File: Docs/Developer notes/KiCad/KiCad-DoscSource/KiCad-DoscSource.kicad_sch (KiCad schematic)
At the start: 0 parts

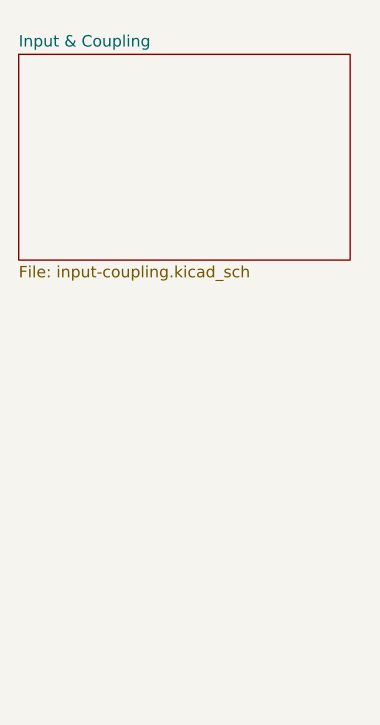
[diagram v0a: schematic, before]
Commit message: Add attenuator to developer notes
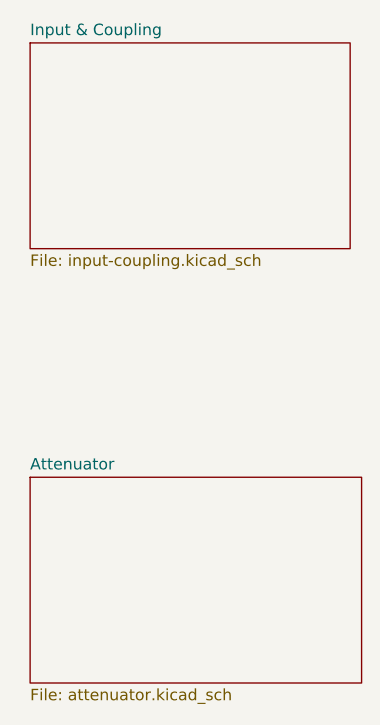
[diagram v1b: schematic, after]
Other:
- added sheet Attenuator (attenuator.kicad_sch)
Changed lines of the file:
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@@
 (kicad_sch (version 20230121) (generator eeschema)
   (paper "A4")
-  (sheet (at 19.05 21.59) (size 36.83 22.86) (fields_autoplaced)
+  (sheet (at 20.32 68.58) (size 36.83 22.86) (fields_autoplaced)
     (stroke (width 0.1524) (type solid))
     (fill (color 0 0 0 0.0000))
-    (property "Sheetname" "Input & Coupling" (at 19.05 20.8784 0)
+    (property "Sheetname" "Attenuator" (at 20.32 67.8684 0)
       (effects (font (size 1.27 1.27)) (justify left bottom))
     )
-    (property "Sheetfile" "input-coupling.kicad_sch" (at 19.05 45.0346 0)
+    (property "Sheetfile" "attenuator.kicad_sch" (at 20.32 92.0246 0)
       (effects (font (size 1.27 1.27)) (justify left top))
     )
+    (instances
+      (project "KiCad-DoscSource"
+        (path "/1d440e8f-b221-47d3-bac2-5e91222a75a8" (page "3"))
+      )
+    )
+  )
+  (sheet (at 20.32 20.32) (size 35.56 22.86) (fields_autoplaced)
+    (stroke (width 0.1524) (type solid))
+    (fill (color 0 0 0 0.0000))
+    (property "Sheetname" "Input & Coupling" (at 20.32 19.6084 0)
+      (effects (font (size 1.27 1.27)) (justify left bottom))
+    )
+    (property "Sheetfile" "input-coupling.kicad_sch" (at 20.32 43.7646 0)
+      (effects (font (size 1.27 1.27)) (justify left top))
+    )
